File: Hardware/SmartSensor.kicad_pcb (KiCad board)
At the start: 2 copper layers, 68.8 x 68.1 mm, 68 parts, among them IC1 VEML7700-TT, IC2 SHTC3, IC3 XB24CZ7PIT-004, IC4 ATECC608B-SSHDA-B, J1 USB_B_Micro, J10 PANTS_1, J11 PANTS_3, J12 PANTS_4, J2 BAT_1, J3 BAT_2, J4 Conn_01x06_Male, J5 Conn_02x05_Odd_Even, J6 Conn_02x05_Odd_Even, J7 Conn_01x02_Male, J8 Conn_01x06_Male, J9 Conn_02x04_Odd_Even, Q1 DMG2301L, U1 TPS63001, U2 CCS811, U3 MCP7940N-xSN, U4 ATmega324PB-AU, Y1 20MHz, Y2 Crystal

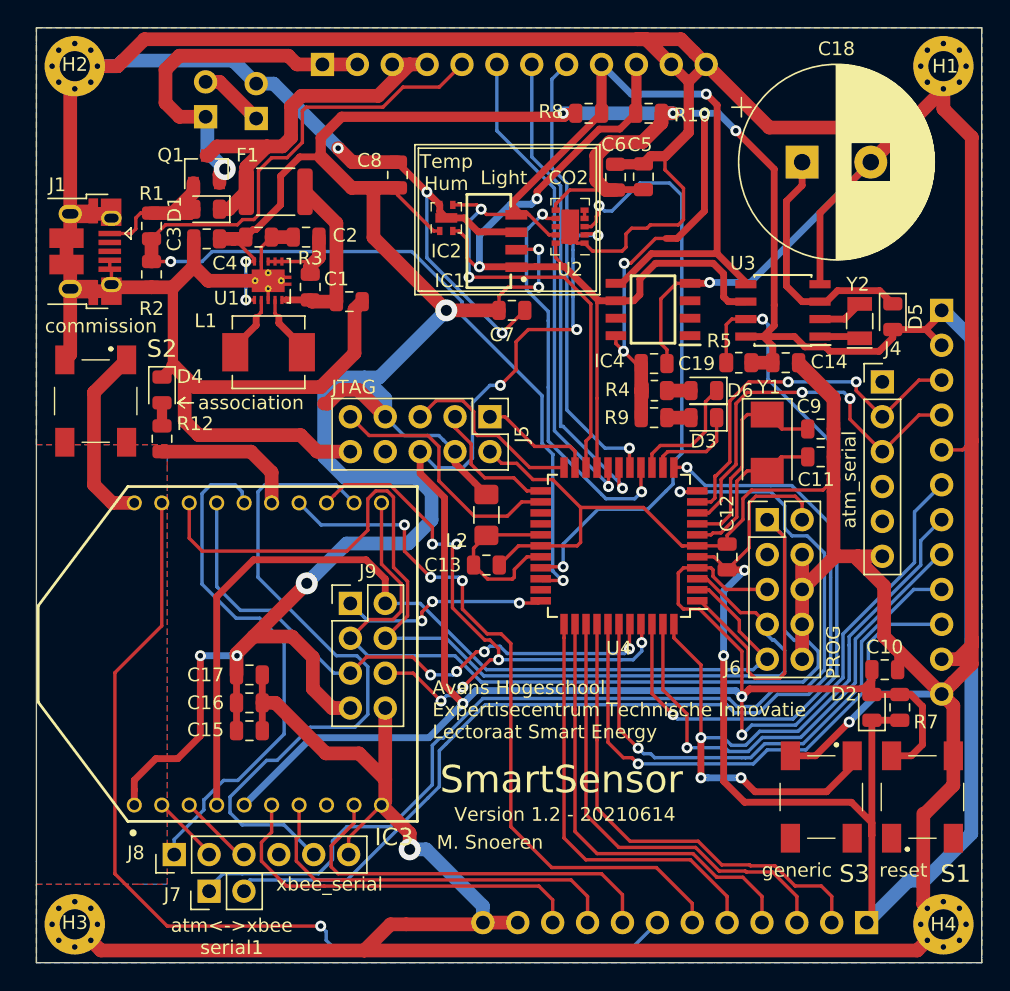
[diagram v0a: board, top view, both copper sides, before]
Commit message: Add custom sensor boards
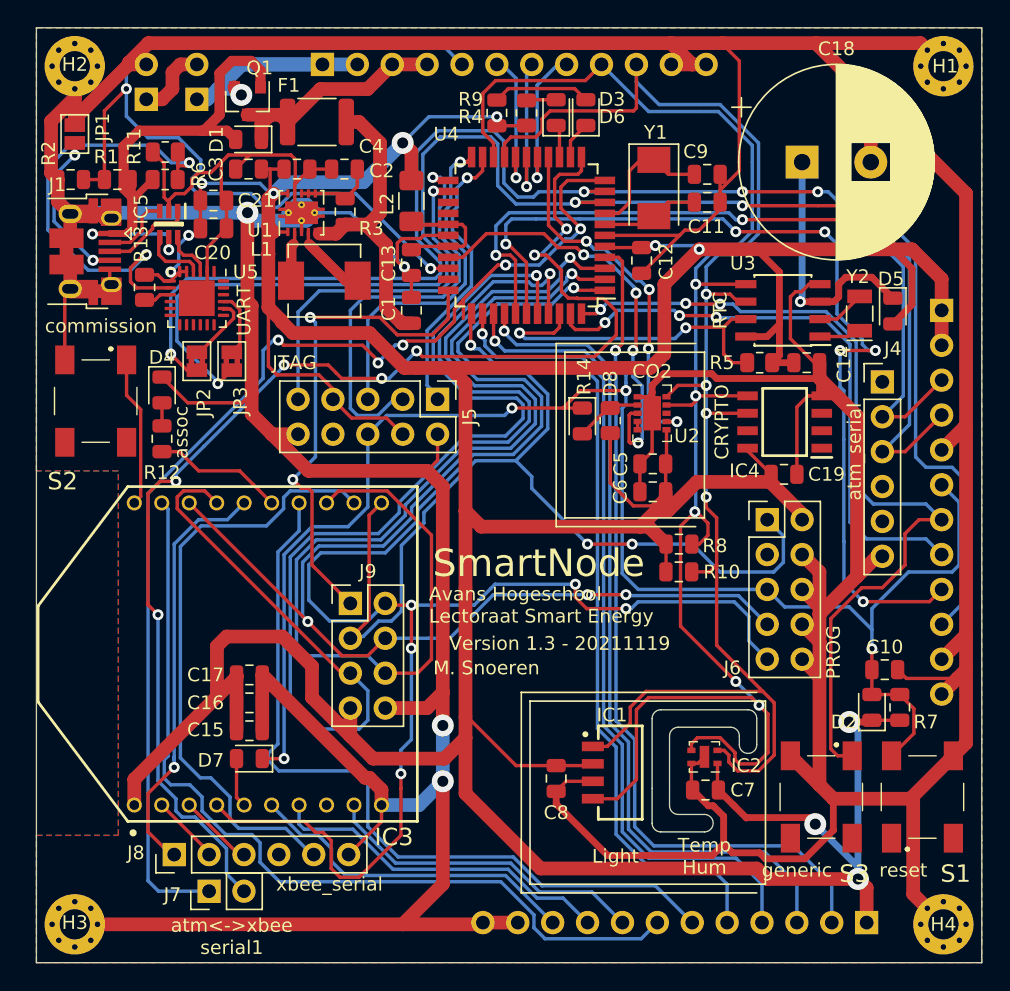
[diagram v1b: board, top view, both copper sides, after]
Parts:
- added C20: 4.7uF, Capacitor_SMD:C_0805_2012Metric, F.Cu at (176.3, 93.2)
- added C21: 100nF, Capacitor_SMD:C_0805_2012Metric, F.Cu at (176.3, 91.2)
- added D7: BAT54???, Diode_SMD:D_0805_2012Metric, F.Cu at (179.0, 131.8)
- added D8: BAT54???, Diode_SMD:D_0805_2012Metric, F.Cu at (203.2, 107.2)
- added IC5: NUF2221W1T2G, SamacSys_Parts:SOT65P210X110-6N, F.Cu at (173.1, 92.9)
- added JP1: ID, Jumper:SolderJumper-2_P1.3mm_Open_Pad1.0x1.5mm, F.Cu at (166.2, 86.3)
- added JP2: DISABLE, Jumper:SolderJumper-2_P1.3mm_Bridged2Bar_Pad1.0x1.5mm, F.Cu at (175.1, 102.9)
- added JP3: DISABLE, Jumper:SolderJumper-2_P1.3mm_Bridged2Bar_Pad1.0x1.5mm, F.Cu at (177.7, 102.9)
- added R11: 47,5K, Resistor_SMD:R_0805_2012Metric, F.Cu at (172.8, 87.7)
- added R13: 1K, Resistor_SMD:R_0805_2012Metric, F.Cu at (171.3, 97.5)
- added R14: 100K, Resistor_SMD:R_0805_2012Metric, F.Cu at (205.2, 107.2)
- added R6: 22,1K, Resistor_SMD:R_0805_2012Metric, F.Cu at (172.8, 89.7)
- added U5: CP2102N-A01-GQFN24, Package_DFN_QFN:QFN-24-1EP_4x4mm_P0.5mm_EP2.6x2.6mm, F.Cu at (175.1, 98.3)
- R12, R4, R9: value 210 -> 330
- moved C8 45.4 mm to (201.3, 133.3), turned to 270 degrees
- moved IC2 43.5 mm to (212.1, 131.7), turned to 180 degrees
- moved C7 37.7 mm to (212.2, 134.1), turned to 180 degrees
- moved R10 33.5 mm to (210.2, 118.2), turned to 0 degrees
- moved IC1 32.5 mm to (204.4, 129.4), turned to 270 degrees
- moved R8 32.1 mm to (210.2, 116.2)
- moved R9 25.0 mm to (197.0, 84.8), turned to 270 degrees
- moved D3 23.8 mm to (203.5, 84.8), turned to 90 degrees
- moved U4 23.6 mm to (199.1, 93.7)
- moved L2 23.5 mm to (190.8, 91.2)
- moved C6 23.1 mm to (208.3, 112.4), turned to 180 degrees
- moved D6 22.9 mm to (201.3, 84.8), turned to 90 degrees
- moved C13 22.7 mm to (190.8, 95.7), turned to 270 degrees
- moved C12 22.5 mm to (207.5, 95.6), turned to 270 degrees
- moved R4 22.3 mm to (199.1, 84.8), turned to 270 degrees
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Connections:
- IC3 pad 5: ATM_RESET -> Net-(D7-Pad2)
- J1 pad 2: Net-(J1-Pad2) -> USB_D-
- J1 pad 3: Net-(J1-Pad3) -> USB_D+
- J1 pad 4: GND -> Net-(J1-Pad4)
- U2 pad 2: ATM_RESET -> Net-(D8-Pad2)
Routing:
- net ATM_RXD_0: track 28.7 -> 103.8 mm, vias 2 -> 4
- net ATM_TXD_0: track 27.5 -> 97.3 mm, vias 2 -> 4
- net ATM_MISO: track 68.7 -> 123.3 mm, vias 0 -> 6
- net XBEE_SPI_SSEL: track 42.8 -> 87.4 mm, vias 4 -> 1
- net SCL: track 63.8 -> 108.0 mm, vias 2 -> 4
- net XBEE_SLEEP: track 45.7 -> 82.1 mm, vias 6 -> 1
- net SDA: track 82.5 -> 117.6 mm, vias 3 -> 5
- net ATM_RESET: track 158.0 -> 123.3 mm, vias 6 -> 5
- net Net-(R11-Pad2): track 0.00 -> 33.5 mm, vias 0 -> 2
- net V_USB: track 10.1 -> 41.8 mm, vias 0 -> 2
- net /Interface/ATM_SDA_1: track 39.6 -> 70.3 mm, vias 1 -> 3
- net /Interface/ATM_SCL_1: track 38.9 -> 69.1 mm, vias 1 -> 6
- net RTC_MFP: track 54.3 -> 25.2 mm
- net /Interface/ATM_PA1: track 33.6 -> 61.8 mm, vias 0 -> 1
- net /Interface/ATM_PA0: track 35.1 -> 63.2 mm, vias 0 -> 1
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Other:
- outline, holes or cut-outs redrawn
- board text added: "AD1"
- board text added: "Avans Hogeschool Lectoraat Smart Energy"
- board text added: "CRYPTO"
- board text added: "D18"
- board text added: "PWM0"
- board text added: "PWM1"
- board text added: "RTC"
- board text added: "SmartNode"
- board text added: "UART"
- board text added: "VREF"
- board text added: "Version 1.3 - 20211119"
- board text added: "XBEE PINS"
- board text added: "assoc"
- board text removed: "Avans Hogeschool Expertisecentrum Technische Innovatie Lectoraat Smart Energy"
- board text removed: "SmartSensor"
- board text removed: "Version 1.2 - 20210614"
- board text removed: "XBEE_AD1"
- board text removed: "XBEE_D18"
- board text removed: "XBEE_PWM0"
- board text removed: "XBEE_PWM1"
- board text removed: "XBEE_VREF"
- board text removed: "association"
